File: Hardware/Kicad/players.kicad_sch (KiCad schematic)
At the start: 13 parts, among them J18 Player1_TM1637, J19 CP TM1637, J20 Player2_TM1637, J7 DE9_Socket, J8 DE9_Socket

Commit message: Inline accessors, small cleanups, removed empty destructors
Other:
- note added: "TM1637's & JOYSTICKS"
- note removed: "PLAYERS & CENTRAL PANEL (except I2C)"
- moved on the sheet: C7, C8, D2, D4, D5, D6, J18, J19, J7

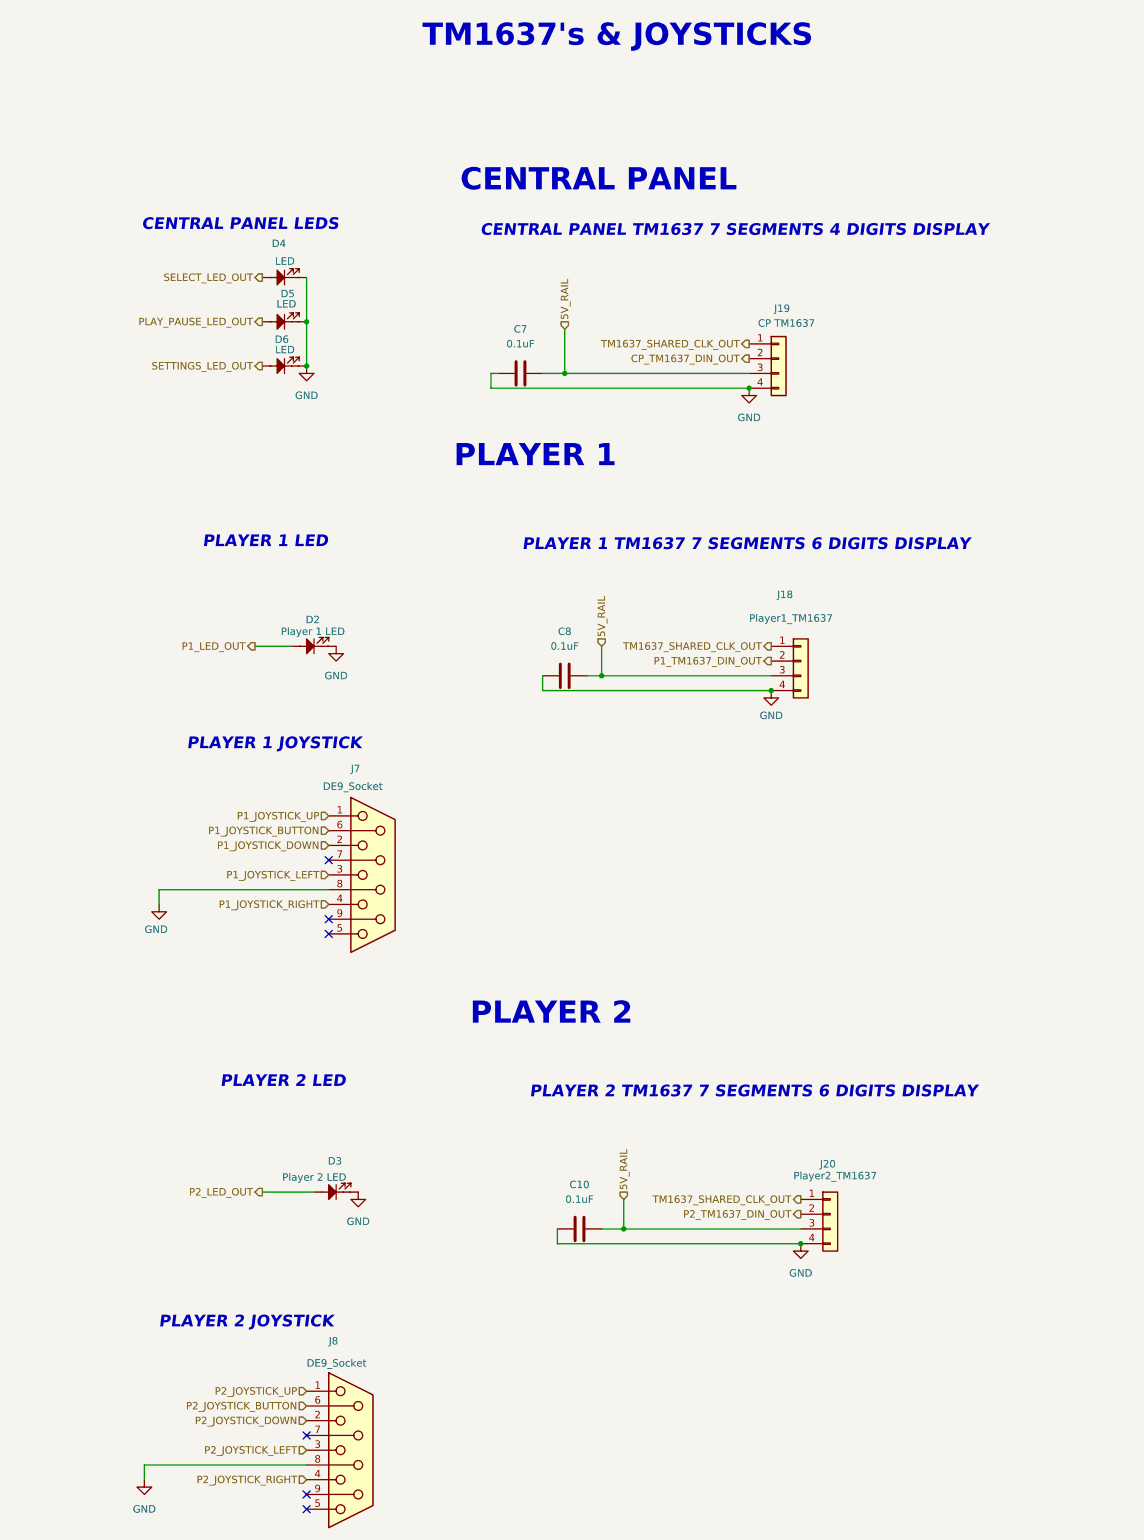
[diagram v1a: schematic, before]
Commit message: Replaced 1602 to 2004 in Kicad and Tinkercad
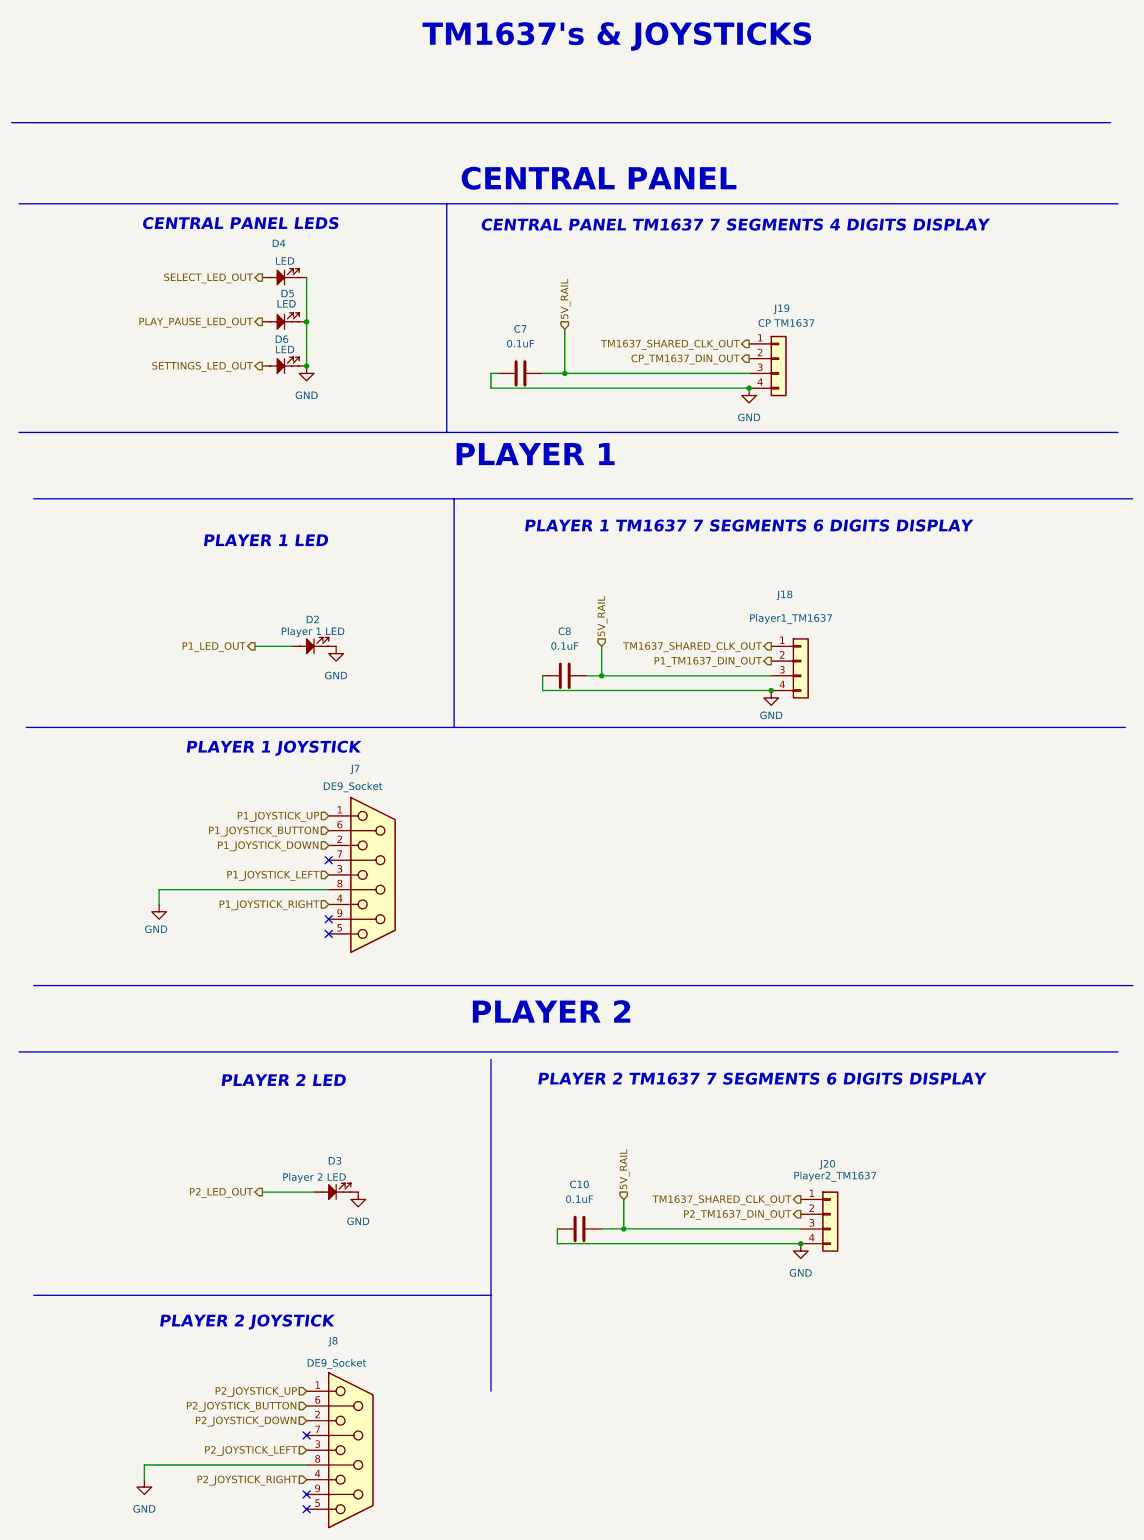
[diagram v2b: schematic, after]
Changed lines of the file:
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@@
 	(text "PLAYER 1 JOYSTICK"
 		(exclude_from_sim no)
-		(at 52.832 142.494 0)
+		(at 52.578 143.256 0)
 		(effects
 			(font
@@
 	(text "CENTRAL PANEL TM1637 7 SEGMENTS 4 DIGITS DISPLAY"
 		(exclude_from_sim no)
-		(at 132.08 54.102 0)
+		(at 132.08 53.34 0)
 		(effects
 			(font
@@
 	(text "PLAYER 2 TM1637 7 SEGMENTS 6 DIGITS DISPLAY\n"
 		(exclude_from_sim no)
-		(at 135.382 202.438 0)
+		(at 136.652 200.406 0)
 		(effects
 			(font
@@
 	(text "PLAYER 1 TM1637 7 SEGMENTS 6 DIGITS DISPLAY"
 		(exclude_from_sim no)
-		(at 134.112 108.204 0)
+		(at 134.366 105.156 0)
 		(effects
 			(font
@@
 		)
 	)
+	(polyline
+		(pts
+			(xy 8.89 194.31) (xy 198.12 194.31)
+		)
+		(stroke
+			(width 0)
+			(type default)
+		)
+	)
+	(polyline
+		(pts
+			(xy 11.43 236.22) (xy 90.17 236.22)
+		)
+		(stroke
+			(width 0)
+			(type default)
+		)
+	)
 	(wire
 		(pts
@@
 		)
 	)
+	(polyline
+		(pts
+			(xy 82.55 87.63) (xy 82.55 48.26)
+		)
+		(stroke
+			(width 0)
+			(type default)
+		)
+	)
 	(wire
 		(pts
@@
 		)
 	)
+	(polyline
+		(pts
+			(xy 90.17 252.73) (xy 90.17 195.58)
+		)
+		(stroke
+			(width 0)
+			(type default)
+		)
+	)
+	(polyline
+		(pts
+			(xy 10.16 138.43) (xy 199.39 138.43)
+		)
+		(stroke
+			(width 0)
+			(type default)
+		)
+	)
 	(wire
 		(pts
@@
 		)
 	)
+	(polyline
+		(pts
+			(xy 8.89 48.26) (xy 198.12 48.26)
+		)
+		(stroke
+			(width 0)
+			(type default)
+		)
+	)
+	(polyline
+		(pts
+			(xy 8.89 87.63) (xy 198.12 87.63)
+		)
+		(stroke
+			(width 0)
+			(type default)
+		)
+	)
 	(wire
 		(pts
@@
 		)
 	)
+	(polyline
+		(pts
+			(xy 83.82 138.43) (xy 83.82 99.06)
+		)
+		(stroke
+			(width 0)
+			(type default)
+		)
+	)
 	(wire
 		(pts
@@
 		)
 	)
+	(polyline
+		(pts
+			(xy 11.43 99.06) (xy 200.66 99.06)
+		)
+		(stroke
+			(width 0)
+			(type default)
+		)
+	)
+	(polyline
+		(pts
+			(xy 7.62 34.29) (xy 196.85 34.29)
+		)
+		(stroke
+			(width 0)
+			(type default)
+		)
+	)
 	(wire
 		(pts
@@
 		)
 		(stroke
+			(width 0)
+			(type default)
+		)
+	)
+	(polyline
+		(pts
+			(xy 11.43 182.88) (xy 200.66 182.88)
+		)
+		(stroke
